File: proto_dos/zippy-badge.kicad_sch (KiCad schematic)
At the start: 37 parts, among them J1 Micro_SD_Card_SPI, J2 USB-C, SW1 Boot Select, SW2 SW_SPDT, U1 NCP115ASN330T2G, U2 RP2040, U3 W25Q32RV, X1 Badgelife_sao_connector_v169b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, Y1 ABM8-272-T3

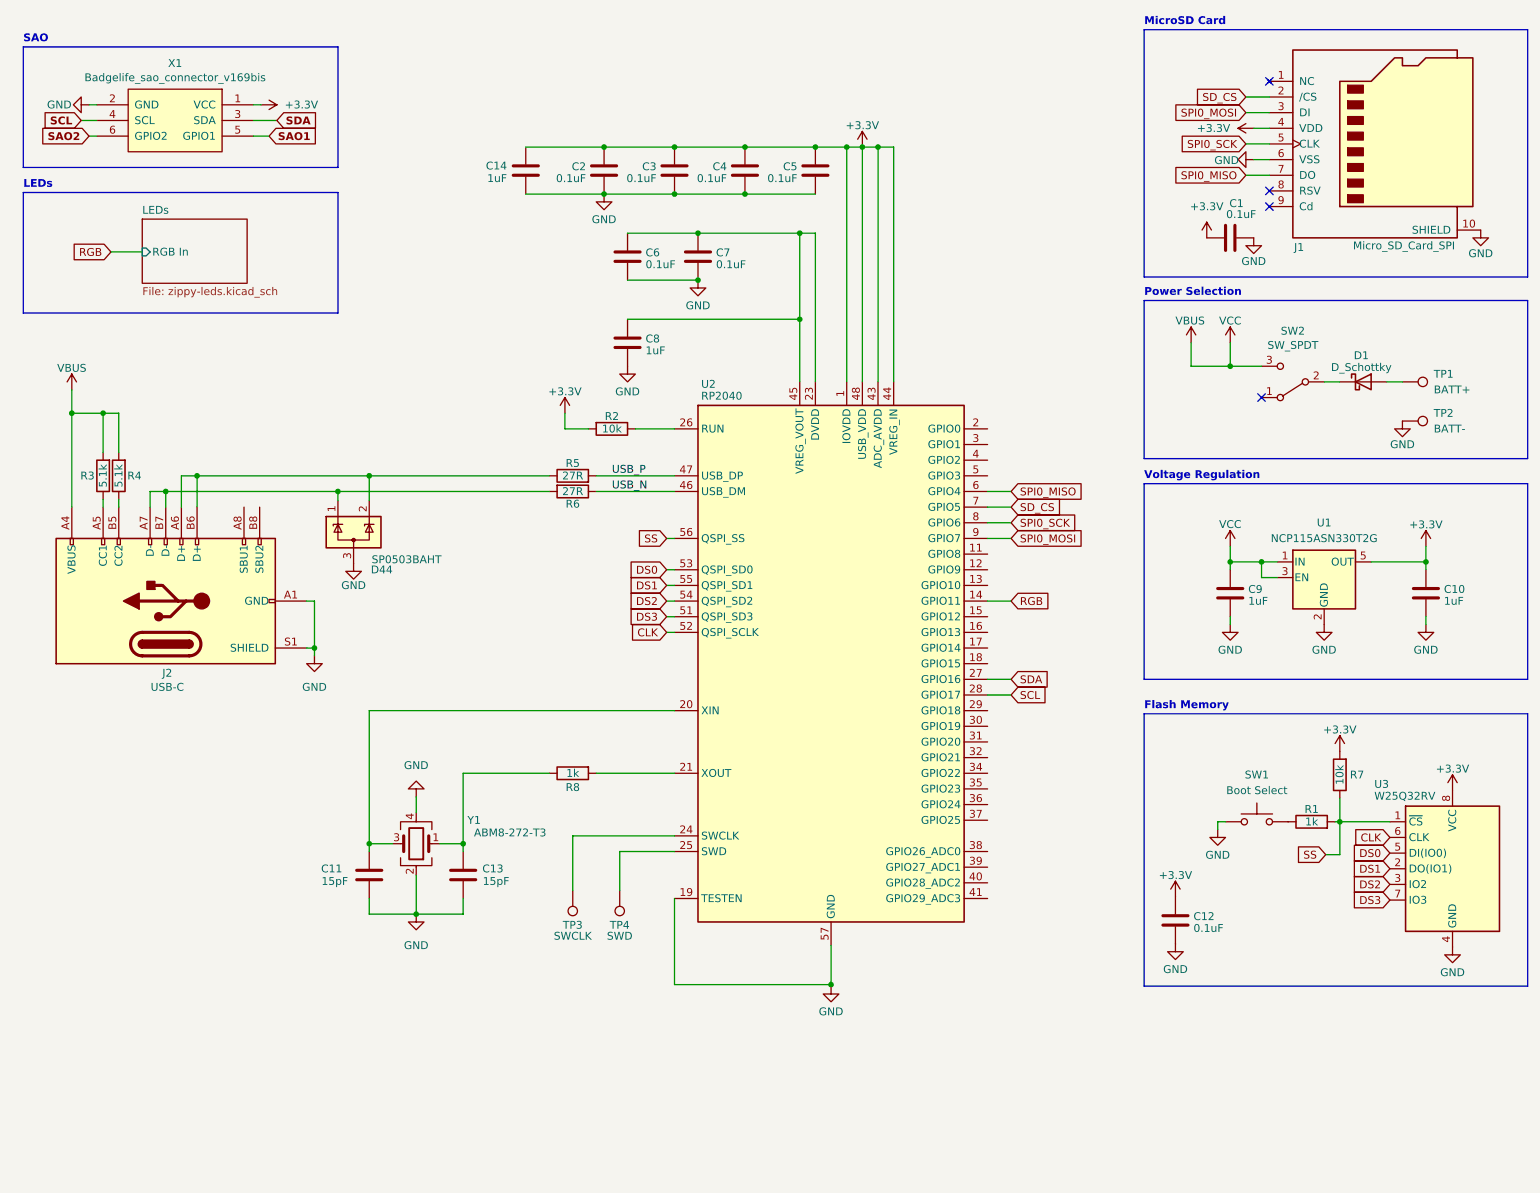
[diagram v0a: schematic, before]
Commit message: Updated proto dos with accelerometer, microphone, and fixed the USB-C CC power detection
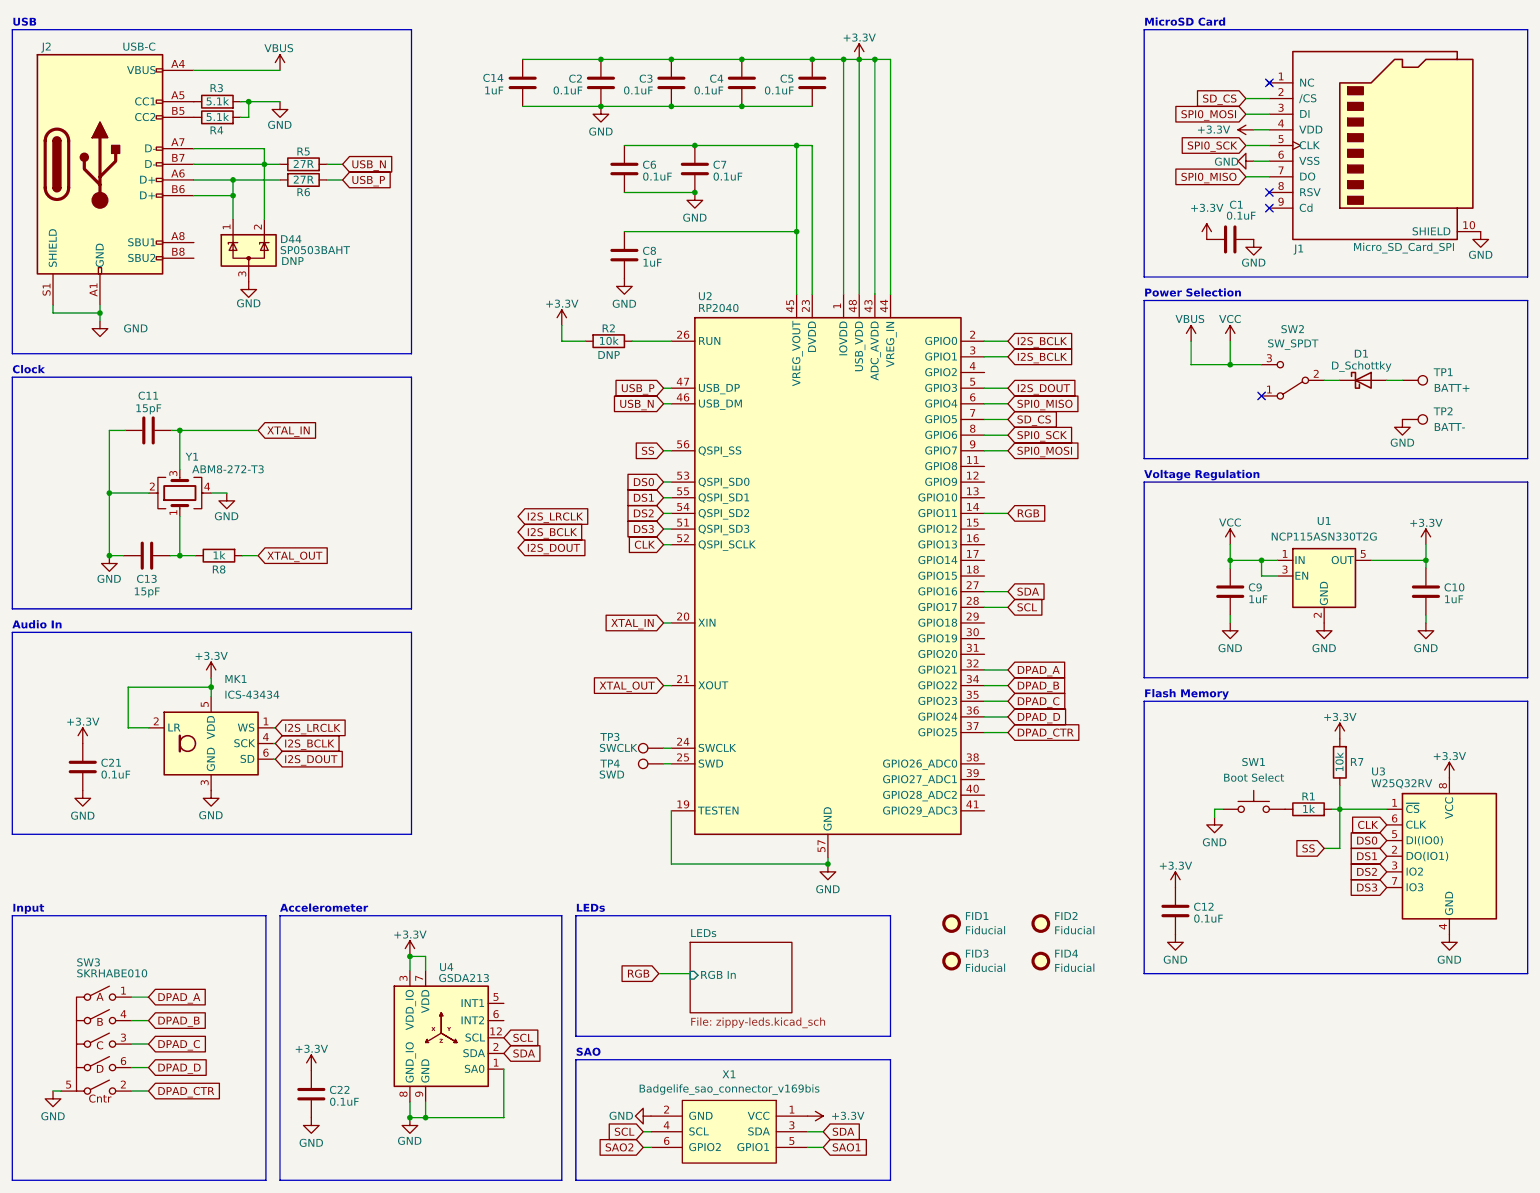
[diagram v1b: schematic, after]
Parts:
- added C21, C22: 0.1uF, Capacitor_SMD:C_0603_1608Metric, symbol Device:C
- added FID1, FID2, FID3, FID4: Fiducial, Fiducial:Fiducial_1mm_Mask2mm, symbol Mechanical:Fiducial
- added MK1: ICS-43434, Sensor_Audio:InvenSense_ICS-43434-6_3.5x2.65mm, symbol Sensor_Audio:ICS-43434
- added SW3: SKRHABE010, symbol SKRHABE010:SKRHABE010
- added U4: GSDA213, Package_LGA:Kionix_LGA-12_2x2mm_P0.5mm_LayoutBorder2x4y, symbol GSDA213:GSDA213
- D44, R2: DNP (none) -> DNP
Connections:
- net +3.3V: now also C21.2, C22.2, MK1.2 (LR), MK1.5 (VDD), U4.3 (VDD_IO), U4.7 (VDD)
- net GND: now also R3.2, R4.2, C21.1, C22.1, MK1.3 (GND), SW3.5 (Common), U4.1 (SA0), U4.8 (GND_IO), U4.9 (GND)
- net SCL: now also U4.12 (SCL)
- net SDA: now also U4.2 (SDA)
- net USB_N: now also R5.2; no longer R6.1
- net USB_P: now also R6.1; no longer R5.2
- net VBUS: no longer R3.2, R4.2
- net XTAL_IN: now reaches C11.2, U2.20 (XIN), Y1.3
- net XTAL_OUT: now reaches R8.2, U2.21 (XOUT)
- net at D44.1 (K), R6.2: now also J2.A6 (D+), J2.B6 (D+); no longer J2.A7 (D-), J2.B7 (D-)
- net at D44.2 (K), R5.1: now also J2.A7 (D-), J2.B7 (D-); no longer J2.A6 (D+), J2.B6 (D+)
- net I2S_BCLK: now reaches U2.2 (GPIO0)
- net I2S_BCLK: now also U2.3 (GPIO1), MK1.4 (SCK)
- net DPAD_A: now reaches U2.32 (GPIO21)
- net DPAD_A: now also SW3.1 (A)
- net DPAD_B: now reaches U2.34 (GPIO22)
- net DPAD_B: now also SW3.4 (B)
- net DPAD_C: now reaches U2.35 (GPIO23)
- net DPAD_C: now also SW3.3 (C)
- net DPAD_D: now reaches U2.36 (GPIO24)
- net DPAD_D: now also SW3.6 (D)
- net DPAD_CTR: now reaches U2.37 (GPIO25)
- net DPAD_CTR: now also SW3.2 (Center)
- net I2S_DOUT: now reaches U2.5 (GPIO3)
- net I2S_DOUT: now also MK1.6 (SD)
- new net I2S_LRCLK: MK1.1 (WS)
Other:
- note added: "Accelerometer"
- note added: "Audio In"
- note added: "Clock"
- note added: "Input"
- note added: "USB"
- moved on the sheet: C11, C12, C13, C14, C2, C3, C4, C5, C6, C7, C8, D44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
